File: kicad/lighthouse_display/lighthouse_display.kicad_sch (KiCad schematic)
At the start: 28 parts, among them J1 Conn_01x12_Pin, U1 IS31FL3731-SA, U2 TPS61176RTER

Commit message: places both led drivers, started routing
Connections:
- net TPS_FB: now reaches R3.1, R4.2, U2.12 (OVP)
- net TPS_SW: now reaches D100.2 (A), L1.2, U2.14 (SW)
- net TPS_VIN: now reaches C11.1, JP1.2 (C), U2.15 (VIN)
- net TPS_MODE: now reaches R1.2, U2.16 (MODE/FAULT)
- net TPS_LDO: now reaches C4.1, U2.2 (VLDO)
- net TPS_ISET: now reaches R2.2, U2.3 (ISET)
- net TPS_COMP: now reaches C3.1, U2.4 (COMP)
- net IS_AD: now reaches R10.2, R8.1, U1.18 (AD)
- net IS_VIN: now reaches C7.1, C8.1, JP2.2 (C), U1.2 (VCC)
- net IS_REXT: now reaches R12.2, U1.6 (R_EXT)
- net IS_FILT: now reaches C6.1, U1.16 (C_FILT)
- net IS_IN: now reaches R11.2, U1.17 (IN)
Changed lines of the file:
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@@
+		)
+	)
+	(label "IS_REXT"
+		(at 91.44 71.12 0)
+		(fields_autoplaced yes)
+		(effects
+			(font
+				(size 1.27 1.27)
+			)
+			(justify left bottom)
+		)
+	)
+	(label "IS_FILT"
+		(at 90.17 66.04 0)
+		(fields_autoplaced yes)
+		(effects
+			(font
+				(size 1.27 1.27)
+			)
+			(justify left bottom)
 		)
 	)
@@
 		)
 	)
+	(label "TPS_SW"
+		(at 119.38 138.43 90)
+		(fields_autoplaced yes)
+		(effects
+			(font
+				(size 1.27 1.27)
+			)
+			(justify left bottom)
+		)
+	)
+	(label "IS_IN"
+		(at 90.17 63.5 0)
+		(fields_autoplaced yes)
+		(effects
+			(font
+				(size 1.27 1.27)
+			)
+			(justify left bottom)
+		)
+	)
+	(label "TPS_LDO"
+		(at 71.12 165.1 0)
+		(fields_autoplaced yes)
+		(effects
+			(font
+				(size 1.27 1.27)
+			)
+			(justify left bottom)
+		)
+	)
+	(label "TPS_VIN"
+		(at 76.2 142.24 0)
+		(fields_autoplaced yes)
+		(effects
+			(font
+				(size 1.27 1.27)
+			)
+			(justify left bottom)
+		)
+	)
 	(label "SCL"
 		(at 66.04 48.26 0)
+		(fields_autoplaced yes)
+		(effects
+			(font
+				(size 1.27 1.27)
+			)
+			(justify left bottom)
+		)
+	)
+	(label "TPS_COMP"
+		(at 58.42 160.02 0)
+		(fields_autoplaced yes)
+		(effects
+			(font
+				(size 1.27 1.27)
+			)
+			(justify left bottom)
+		)
+	)
+	(label "TPS_ISET"
+		(at 81.28 170.18 0)
+		(fields_autoplaced yes)
+		(effects
+			(font
+				(size 1.27 1.27)
+			)
+			(justify left bottom)
+		)
+	)
+	(label "TPS_MODE"
+		(at 48.26 154.94 0)
 		(fields_autoplaced yes)
 		(effects
@@
 		)
 	)
+	(label "IS_VIN"
+		(at 97.79 30.48 0)
+		(fields_autoplaced yes)
+		(effects
+			(font
+				(size 1.27 1.27)
+			)
+			(justify left bottom)
+		)
+	)
 	(label "~{INTB}"
 		(at 66.04 58.42 0)
 		(fields_autoplaced yes)
 		(effects
+			(font
+				(size 1.27 1.27)
+			)
+			(justify left bottom)
+		)
+	)
+	(label "IS_AD"
+		(at 90.17 50.8 0)
+		(fields_autoplaced yes)
+		(effects
+			(font
+				(size 1.27 1.27)
+			)
+			(justify left bottom)
+		)
+	)
+	(label "TPS_FB"
+		(at 121.92 147.32 0)
+		(fields_autoplaced yes)
+		(effects

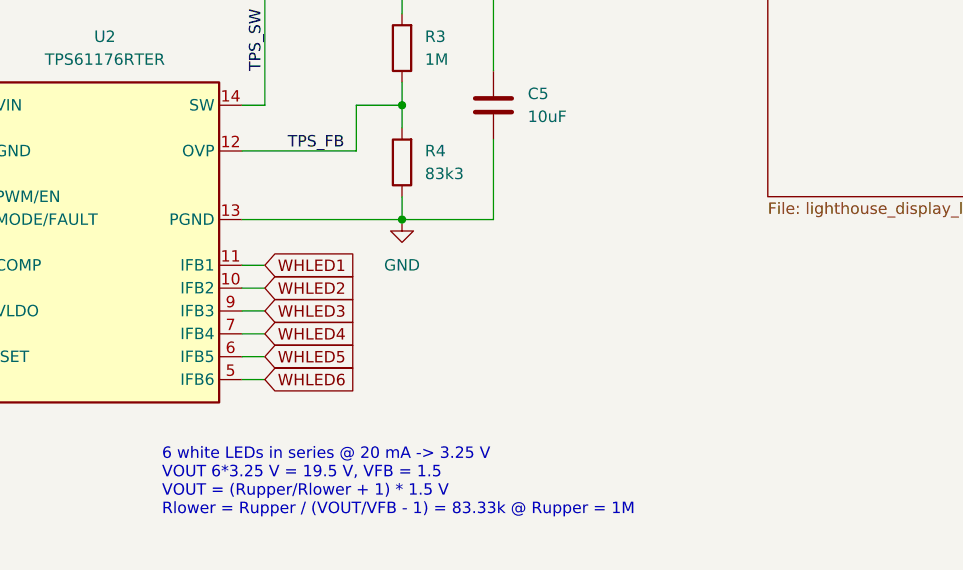
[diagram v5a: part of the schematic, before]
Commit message: use 7*6 white LEDs in a row now, almost all leds connected
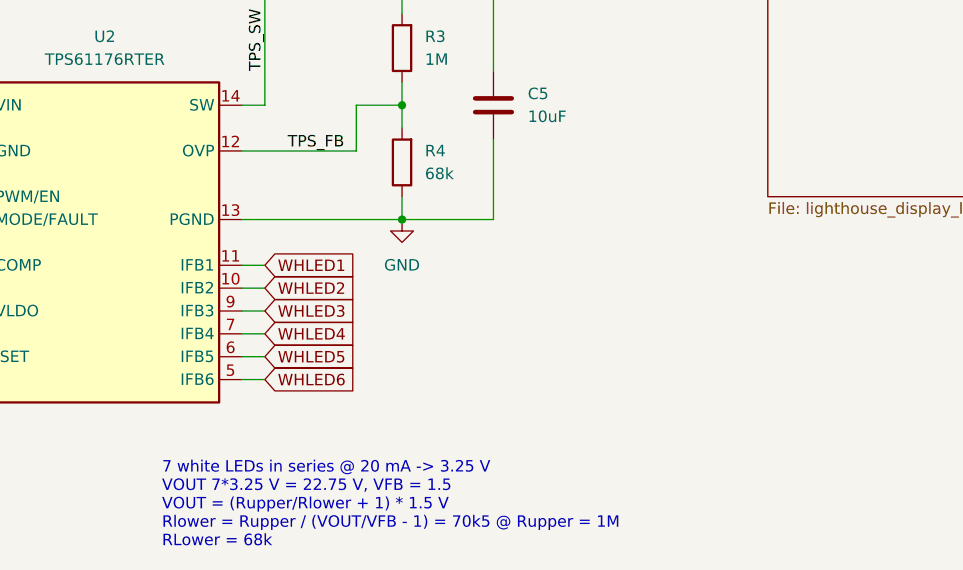
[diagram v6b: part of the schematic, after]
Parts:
- R4: value 83k3 -> 68k
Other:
- note added: "7 white LEDs in series @ 20 mA -> 3.25 V VOUT 7*3.25 V = 22.75 V, VFB = 1.5 VOUT = (Rupper/Rlower + 1) * 1.5 V Rlower = Rupper / (VOUT/VFB - 1) = 70k5 @ Rupper = 1M RLower = 68k"
- note removed: "6 white LEDs in series @ 20 mA -> 3.25 V VOUT 6*3.25 V = 19.5 V, VFB = 1.5 VOUT = (Rupper/Rlower + 1) * 1.5 V Rlower = Rupper / (VOUT/VFB - 1) = 83.33k @ Rupper = 1M"
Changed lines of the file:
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@@
 		)
 	)
-	(text "6 white LEDs in series @ 20 mA -> 3.25 V\nVOUT 6*3.25 V = 19.5 V, VFB = 1.5\nVOUT = (Rupper/Rlower + 1) * 1.5 V\nRlower = Rupper / (VOUT/VFB - 1) = 83.33k @ Rupper = 1M"
-		(exclude_from_sim no)
-		(at 107.95 184.15 0)
+	(text "7 white LEDs in series @ 20 mA -> 3.25 V\nVOUT 7*3.25 V = 22.75 V, VFB = 1.5\nVOUT = (Rupper/Rlower + 1) * 1.5 V\nRlower = Rupper / (VOUT/VFB - 1) = 70k5 @ Rupper = 1M\nRLower = 68k"
+		(exclude_from_sim no)
+		(at 107.95 186.69 0)
 		(effects
 			(font
@@
 			)
 		)
-		(property "Value" "83k3"
+		(property "Value" "68k"
 			(at 137.16 149.8599 0)
 			(effects

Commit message: 100% routed
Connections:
- net GND: now also U2.17 (PGND)
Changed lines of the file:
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@@
+	)
+	(junction
+		(at 120.65 154.94)
+		(diameter 0)
+		(color 0 0 0 0)
 	)
 	(junction
@@
 	(wire
 		(pts
+			(xy 116.84 157.48) (xy 120.65 157.48)
+		)
+		(stroke
+			(width 0)
+			(type default)
+		)
+	)
+	(wire
+		(pts
 			(xy 86.36 50.8) (xy 96.52 50.8)
 		)
@@
 	(wire
 		(pts
-			(xy 116.84 154.94) (xy 134.62 154.94)
+			(xy 116.84 154.94) (xy 120.65 154.94)
 		)
 		(stroke
@@
 	(wire
 		(pts
+			(xy 120.65 154.94) (xy 134.62 154.94)
+		)
+		(stroke
+			(width 0)
+			(type default)
+		)
+	)
+	(wire
+		(pts
 			(xy 58.42 179.07) (xy 71.12 179.07)
 		)
@@
 		(pts
 			(xy 119.38 127) (xy 121.92 127)
+		)
+		(stroke
+			(width 0)
+			(type default)
+		)
+	)
+	(wire
+		(pts
+			(xy 120.65 154.94) (xy 120.65 157.48)
 		)
 		(stroke
@@
 		(pin "1"
 		)
+		(pin "17"
+		)
 		(instances

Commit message: hardware for lighthouse display rev1 and button rev1 done
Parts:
- added C9: 100nF, Capacitor_SMD:C_0603_1608Metric_Pad1.08x0.95mm_HandSolder, symbol Device:C
- added U3: SHTC3, Sensor_Humidity:Sensirion_DFN-4-1EP_2x2mm_P1mm_EP0.7x1.6mm, symbol Sensor_Humidity:SHTC3
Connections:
- net +3.3V: now also C9.1, U3.1 (VDD)
- net GND: now also C9.2, U3.4 (VSS)
- net SCL: now also U3.2 (SCL)
- net SDA: now also U3.3 (SDA)
